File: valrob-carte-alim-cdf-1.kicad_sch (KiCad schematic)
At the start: 35 parts, among them J1 USB_C_Receptacle_USB2.0_14P, J26 Conn_01x02, J6 Conn_01x04_Pin, SW1 SW_Push, SW2 SW_Push, SW3 SW_Push, U3 SN65HVD230, U4 ESP32-S3-WROOM-1

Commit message: schem: complete BOM
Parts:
- C4: JLCPCB Part # C1525 -> C307331; Manufacturer Part Number CL05B104KO5NNNC -> CL05B104KB54PNC
- U4: Basic (none) -> Z; JLCPCB Part # (none) -> C2913204; Manufacturer (none) -> Espressif; Manufacturer Part Number (none) -> ESP32-S3-WROOM-1-N8R2
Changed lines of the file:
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@@
+			)
+		)
+		(property "Basic" "Z"
+			(at 137.16 104.14 0)
+			(effects
+				(font
+					(size 1.27 1.27)
+				)
+				(hide yes)
+			)
+		)
+		(property "JLCPCB Part #" "C2913204"
+			(at 137.16 104.14 0)
+			(effects
+				(font
+					(size 1.27 1.27)
+				)
+				(hide yes)
+			)
+		)
+		(property "Manufacturer" "Espressif"
+			(at 137.16 104.14 0)
+			(effects
+				(font
+					(size 1.27 1.27)
+				)
+				(hide yes)
+			)
+		)
+		(property "Manufacturer Part Number" "ESP32-S3-WROOM-1-N8R2"
+			(at 137.16 104.14 0)
+			(effects
+				(font
+					(size 1.27 1.27)
+				)
+				(hide yes)
 			)
 		)
@@
 			)
 		)
-		(property "JLCPCB Part #" "C1525"
+		(property "JLCPCB Part #" "C307331"
 			(at 127 181.61 0)
 			(effects
@@
 			)
 		)
-		(property "Manufacturer Part Number" "CL05B104KO5NNNC"
+		(property "Manufacturer Part Number" "CL05B104KB54PNC"
 			(at 127 181.61 0)
 			(effects

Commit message: schem: add sheet title
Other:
- company: (none) -> Valrobotik
- title: (none) -> Carte alim CDF 1
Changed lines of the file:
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@@
 	(generator_version "9.0")
 	(paper "A4")
+	(title_block
+		(title "Carte alim CDF 1")
+		(date "2026-01-15")
+		(rev "01")
+		(company "Valrobotik")
+	)
 	(rectangle
 		(start 15.24 119.38)

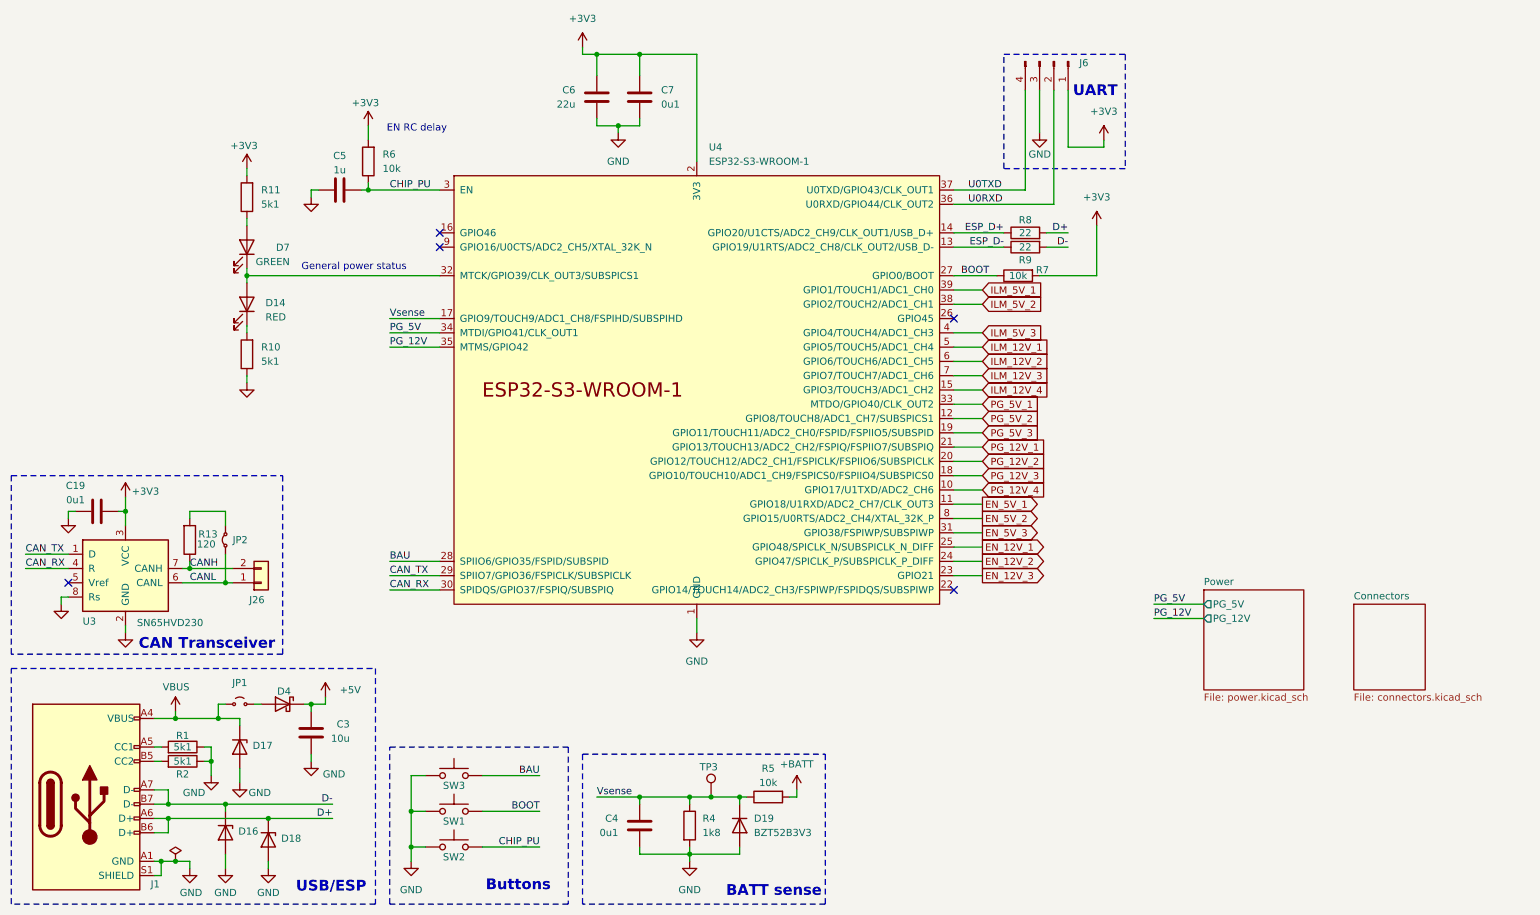
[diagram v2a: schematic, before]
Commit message: schem: renumber
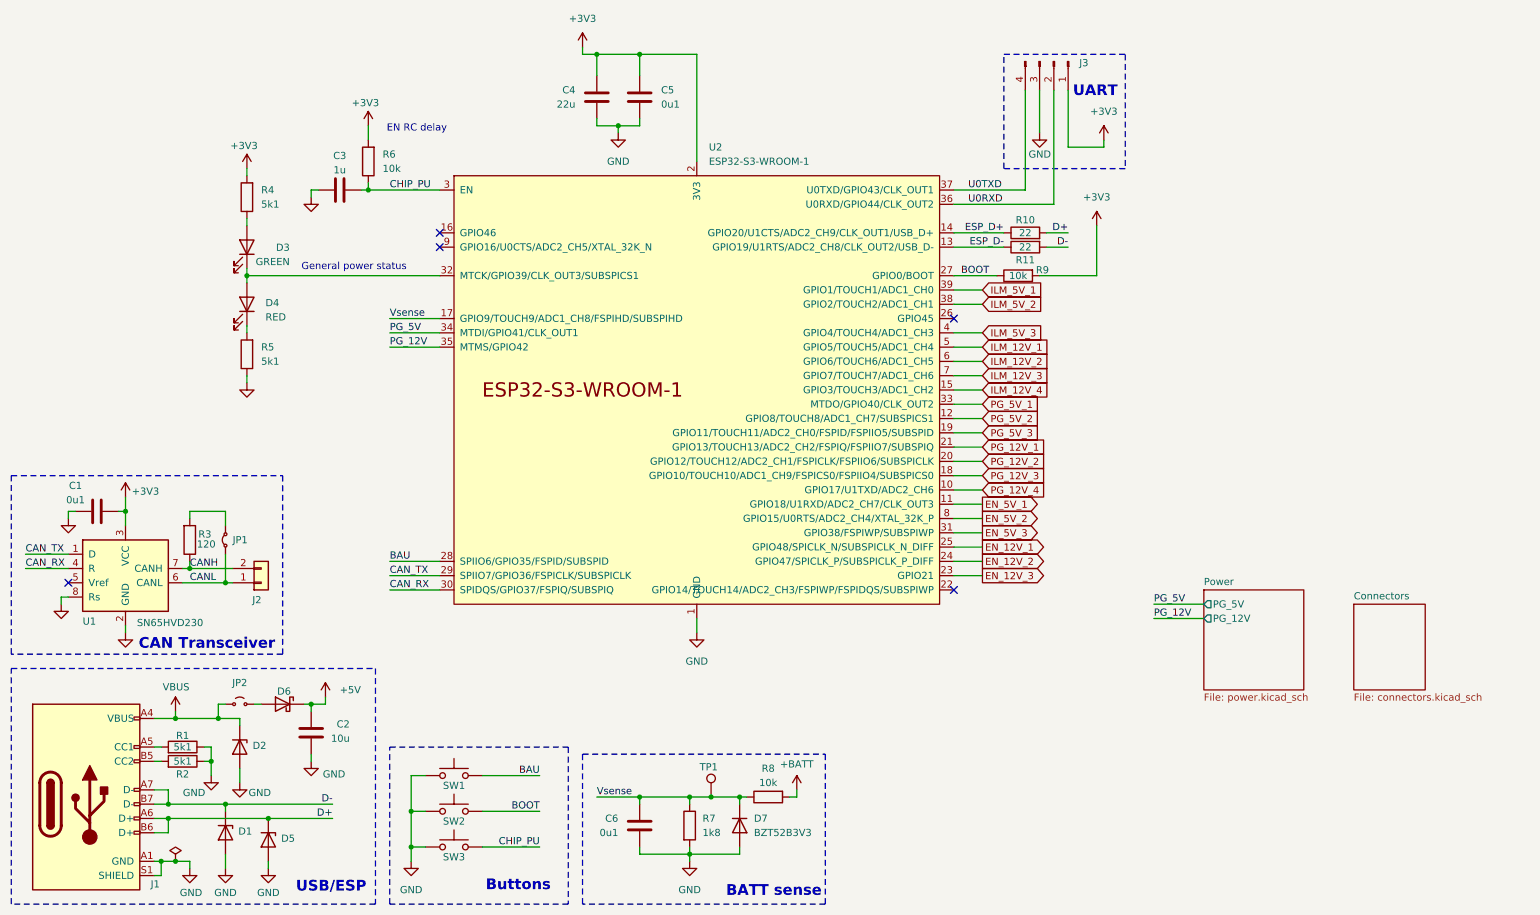
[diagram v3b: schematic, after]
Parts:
- renumbered C19 to C1, C3 to C2, C5 to C3, C6 to C4, C7 to C5, C4 to C6, D16 to D1, D17 to D2, D7 to D3, D14 to D4, D18 to D5, D4 to D6, D19 to D7, J26 to J2, J6 to J3, JP2 to JP1, JP1 to JP2, R8 to R10, R9 to R11, R13 to R3, R11 to R4, R10 to R5, R4 to R7, R5 to R8, R7 to R9, SW3 to SW1, SW1 to SW2, SW2 to SW3, TP3 to TP1, U3 to U1, U4 to U2

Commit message: pcb: add initial rough layout
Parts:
- SW2, SW3: footprint Connector_JST:JST_XH_B2B-XH-A_1x02_P2.50mm_Vertical -> Button_Switch_SMD:SW_SPST_TS-1088-xR020; Basic Z -> Y; JLCPCB Part # C158012 -> C720477; Manufacturer JST -> XUNPU; Manufacturer Part Number B2B-XH-A(LF)(SN) -> TS-1088-AR02016
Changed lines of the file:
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@@
-	)
-	(symbol
-		(lib_id "Switch:SW_Push")
-		(at 93.98 185.42 0)
-		(unit 1)
-		(exclude_from_sim no)
-		(in_bom yes)
-		(on_board yes)
-		(dnp no)
-		(property "Reference" "SW3"
-			(at 93.98 187.198 0)
-			(effects
-				(font
-					(size 1.27 1.27)
-				)
-			)
-		)
-		(property "Value" "SW_Push"
-			(at 93.98 180.34 0)
-			(effects
-				(font
-					(size 1.27 1.27)
-				)
-				(hide yes)
-			)
-		)
-		(property "Footprint" "Connector_JST:JST_XH_B2B-XH-A_1x02_P2.50mm_Vertical"
-			(at 93.98 180.34 0)
-			(effects
-				(font
-					(size 1.27 1.27)
-				)
-				(hide yes)
-			)
-		)
-		(property "Datasheet" "~"
-			(at 93.98 180.34 0)
-			(effects
-				(font
-					(size 1.27 1.27)
-				)
-				(hide yes)
-			)
-		)
-		(property "Description" "Push button switch, generic, two pins"
-			(at 93.98 185.42 0)
-			(effects
-				(font
-					(size 1.27 1.27)
-				)
-				(hide yes)
-			)
-		)
-		(property "Manufacturer" "JST"
-			(at 93.98 185.42 0)
-			(effects
-				(font
-					(size 1.27 1.27)
-				)
-				(hide yes)
-			)
-		)
-		(property "Manufacturer Part Number" "B2B-XH-A(LF)(SN)"
-			(at 93.98 185.42 0)
-			(effects
-				(font
-					(size 1.27 1.27)
-				)
-				(hide yes)
-			)
-		)
-		(property "Basic" "Z"
-			(at 93.98 185.42 0)
-			(effects
-				(font
-					(size 1.27 1.27)
-				)
-				(hide yes)
-			)
-		)
-		(property "JLCPCB Part #" "C158012"
-			(at 93.98 185.42 0)
-			(effects
-				(font
-					(size 1.27 1.27)
-				)
-				(hide yes)
-			)
-		)
-		(pin "2"
-		)
-		(pin "1"
-		)
-		(instances
-			(project "valrob-carte-alim-cdf-1"
-				(path "/8d7b287d-627f-46aa-8c27-0b5ed29ab4a2"
-					(reference "SW3")
-					(unit 1)
-				)
-			)
-		)
 	)
 	(symbol
@@
 	)
 	(symbol
+		(lib_id "Switch:SW_Push")
+		(at 93.98 179.07 0)
+		(unit 1)
+		(exclude_from_sim no)
+		(in_bom yes)
+		(on_board yes)
+		(dnp no)
+		(property "Reference" "SW2"
+			(at 93.98 180.848 0)
+			(effects
+				(font
+					(size 1.27 1.27)
+				)
+			)
+		)
+		(property "Value" "SW_Push"
+			(at 93.98 173.99 0)
+			(effects
+				(font
+					(size 1.27 1.27)
+				)
+				(hide yes)
+			)
+		)
+		(property "Footprint" "Button_Switch_SMD:SW_SPST_TS-1088-xR020"
+			(at 93.98 173.99 0)
+			(effects
+				(font
+					(size 1.27 1.27)
+				)
+				(hide yes)
+			)
+		)
+		(property "Datasheet" "~"
+			(at 93.98 173.99 0)
+			(effects
+				(font
+					(size 1.27 1.27)
+				)
+				(hide yes)
+			)
+		)
+		(property "Description" "Push button switch, generic, two pins"
+			(at 93.98 179.07 0)
+			(effects
+				(font
+					(size 1.27 1.27)
+				)
+				(hide yes)
+			)
+		)
+		(property "Manufacturer" "XUNPU"
+			(at 93.98 179.07 0)
+			(effects
+				(font
+					(size 1.27 1.27)
+				)
+				(hide yes)
+			)
+		)
+		(property "Manufacturer Part Number" "TS-1088-AR02016"
+			(at 93.98 179.07 0)
+			(effects
+				(font
+					(size 1.27 1.27)
+				)
+				(hide yes)
+			)
+		)
+		(property "Basic" "Y"
+			(at 93.98 179.07 0)
+			(effects
+				(font
+					(size 1.27 1.27)
+				)
+				(hide yes)
+			)
+		)
+		(property "JLCPCB Part #" "C720477"
+			(at 93.98 179.07 0)
+			(effects
+				(font
+					(size 1.27 1.27)
+				)
+				(hide yes)
+			)
+		)
+		(pin "2"
+		)
+		(pin "1"
+		)
+		(instances
+			(project "valrob-carte-alim-cdf-1"
+				(path "/8d7b287d-627f-46aa-8c27-0b5ed29ab4a2"
+					(reference "SW2")
+					(unit 1)
+				)
+			)
+		)
+	)
+	(symbol
 		(lib_id "Connector_Generic:Conn_01x02")
 		(at 59.69 138.43 0)
@@
 	)
 	(symbol
-		(lib_id "Switch:SW_Push")
-		(at 93.98 179.07 0)
-		(unit 1)
-		(exclude_from_sim no)
-		(in_bom yes)
-		(on_board yes)
-		(dnp no)
-		(property "Reference" "SW2"
-			(at 93.98 180.848 0)
-			(effects
-				(font
-					(size 1.27 1.27)
-				)
-			)
-		)
-		(property "Value" "SW_Push"
-			(at 93.98 173.99 0)
-			(effects
-				(font
-					(size 1.27 1.27)
-				)
-				(hide yes)
-			)
-		)
-		(property "Footprint" "Connector_JST:JST_XH_B2B-XH-A_1x02_P2.50mm_Vertical"
-			(at 93.98 173.99 0)
-			(effects
-				(font
-					(size 1.27 1.27)
-				)
-				(hide yes)
-			)
-		)
-		(property "Datasheet" "~"
-			(at 93.98 173.99 0)
-			(effects
-				(font
-					(size 1.27 1.27)
-				)
-				(hide yes)
-			)
-		)
-		(property "Description" "Push button switch, generic, two pins"
-			(at 93.98 179.07 0)
-			(effects
-				(font
-					(size 1.27 1.27)
-				)
-				(hide yes)
-			)
-		)
-		(property "Manufacturer" "JST"
-			(at 93.98 179.07 0)
-			(effects
-				(font
-					(size 1.27 1.27)
-				)
-				(hide yes)
-			)
-		)
-		(property "Manufacturer Part Number" "B2B-XH-A(LF)(SN)"
-			(at 93.98 179.07 0)
-			(effects
-				(font
-					(size 1.27 1.27)
-				)
-				(hide yes)
-			)
-		)
-		(property "Basic" "Z"
-			(at 93.98 179.07 0)
-			(effects
-				(font
-					(size 1.27 1.27)
-				)
-				(hide yes)
-			)
-		)
-		(property "JLCPCB Part #" "C158012"
-			(at 93.98 179.07 0)
-			(effects
-				(font
-					(size 1.27 1.27)
-				)
-				(hide yes)
-			)
-		)
-		(pin "2"
-		)
-		(pin "1"
-		)
-		(instances
-			(project "valrob-carte-alim-cdf-1"
-				(path "/8d7b287d-627f-46aa-8c27-0b5ed29ab4a2"
-					(reference "SW2")
-					(unit 1)
-				)
-			)
-		)
-	)
-	(symbol
 		(lib_id "power:GND")
 		(at 55.88 173.99 0)
@@
 					(unit 1)
 				)
+			)
+		)
+	)
+	(symbol
+		(lib_id "Switch:SW_Push")
+		(at 93.98 185.42 0)
+		(unit 1)
+		(exclude_from_sim no)
+		(in_bom yes)
+		(on_board yes)
+		(dnp no)
+		(property "Reference" "SW3"
+			(at 93.98 187.198 0)
+			(effects
+				(font
+					(size 1.27 1.27)
+				)
+			)
+		)
+		(property "Value" "SW_Push"
+			(at 93.98 180.34 0)
+			(effects
+				(font
+					(size 1.27 1.27)
+				)
+				(hide yes)
+			)
+		)
+		(property "Footprint" "Button_Switch_SMD:SW_SPST_TS-1088-xR020"
+			(at 93.98 180.34 0)
+			(effects
+				(font
+					(size 1.27 1.27)
+				)
+				(hide yes)
+			)
+		)
+		(property "Datasheet" "~"
+			(at 93.98 180.34 0)
+			(effects
+				(font
+					(size 1.27 1.27)
+				)
+				(hide yes)
+			)
+		)
+		(property "Description" "Push button switch, generic, two pins"
+			(at 93.98 185.42 0)
+			(effects
+				(font
+					(size 1.27 1.27)
+				)
+				(hide yes)
+			)
+		)
+		(property "Manufacturer" "XUNPU"
+			(at 93.98 185.42 0)
+			(effects
+				(font
+					(size 1.27 1.27)
+				)
+				(hide yes)
+			)
+		)
+		(property "Manufacturer Part Number" "TS-1088-AR02016"
+			(at 93.98 185.42 0)
+			(effects
+				(font
+					(size 1.27 1.27)
+				)
+				(hide yes)
+			)
+		)
+		(property "Basic" "Y"
+			(at 93.98 185.42 0)
+			(effects
+				(font
+					(size 1.27 1.27)
+				)
+				(hide yes)
+			)
+		)
+		(property "JLCPCB Part #" "C720477"
+			(at 93.98 185.42 0)
+			(effects
+				(font
+					(size 1.27 1.27)
+				)
+				(hide yes)
+			)
+		)
+		(pin "2"
+		)
+		(pin "1"
+		)
+		(instances
+			(project "valrob-carte-alim-cdf-1"
+				(path "/8d7b287d-627f-46aa-8c27-0b5ed29ab4a2"
+					(reference "SW3")
+					(unit 1)
+				)

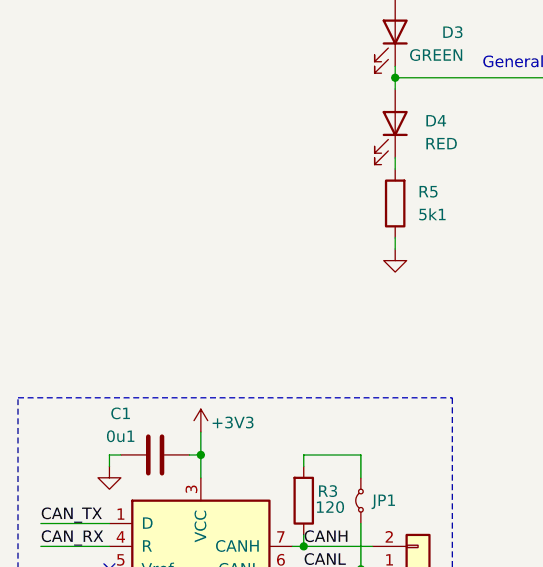
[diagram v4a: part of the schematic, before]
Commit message: schem: add mounting holes
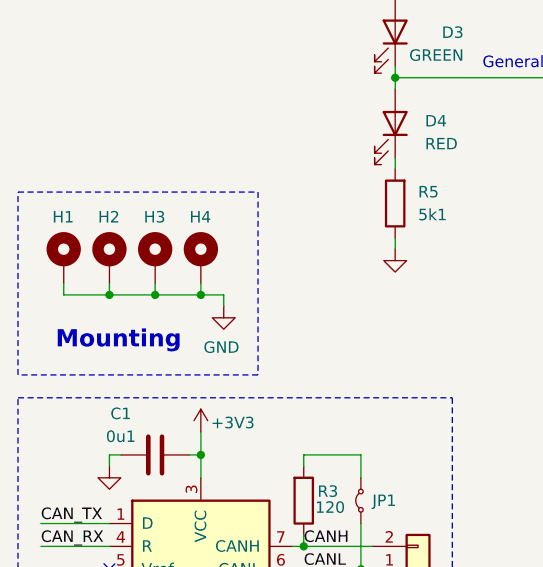
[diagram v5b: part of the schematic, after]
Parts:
- added H1, H2, H3, H4: MountingHole_Pad, MountingHole:MountingHole_2.2mm_M2_Pad_Via, symbol Mechanical:MountingHole_Pad
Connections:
- net GND: now also H1.1, H2.1, H3.1, H4.1
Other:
- note added: "Mounting"

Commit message: pcb: add can layout
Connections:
- net CAN_RX: now also U2.29 (SPIIO7/GPIO36/FSPICLK/SUBSPICLK); no longer U2.30 (SPIDQS/GPIO37/FSPIQ/SUBSPIQ)
- net CAN_TX: now also U2.30 (SPIDQS/GPIO37/FSPIQ/SUBSPIQ); no longer U2.29 (SPIIO7/GPIO36/FSPICLK/SUBSPICLK)
- net VBUS: no longer D2.1 (K)
- net at D6.2 (A), JP2.2 (B): now also D2.1 (K)
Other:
- moved on the sheet: JP2
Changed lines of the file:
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@@
 	)
 	(junction
-		(at 52.07 162.56)
-		(diameter 0)
-		(color 0 0 0 0)
-	)
-	(junction
 		(at 86.36 185.42)
 		(diameter 0)
@@
 	)
 	(junction
-		(at 44.45 162.56)
-		(diameter 0)
-		(color 0 0 0 0)
-	)
-	(junction
 		(at 46.99 135.89)
 		(diameter 0)
@@
 	)
 	(junction
+		(at 44.45 162.56)
+		(diameter 0)
+		(color 0 0 0 0)
+	)
+	(junction
 		(at 78.74 68.58)
 		(diameter 0)
@@
 		(color 0 0 0 0)
 	)
+	(junction
+		(at 55.88 162.56)
+		(diameter 0)
+		(color 0 0 0 0)
+	)
 	(no_connect
 		(at 91.44 76.2)
@@
 	(wire
 		(pts
-			(xy 52.07 160.02) (xy 53.34 160.02)
-		)
-		(stroke
-			(width 0)
-			(type default)
-		)
-	)
-	(wire
-		(pts
 			(xy 35.56 146.05) (xy 35.56 147.32)
 		)
@@
 	(wire
 		(pts
+			(xy 55.88 160.02) (xy 59.69 160.02)
+		)
+		(stroke
+			(width 0)
+			(type default)
+		)
+	)
+	(wire
+		(pts
 			(xy 182.88 114.3) (xy 187.96 114.3)
 		)
@@
 	(wire
 		(pts
+			(xy 82.55 137.16) (xy 91.44 137.16)
+		)
+		(stroke
+			(width 0)
+			(type default)
+		)
+	)
+	(wire
+		(pts
+			(xy 44.45 162.56) (xy 48.26 162.56)
+		)
+		(stroke
+			(width 0)
+			(type default)
+		)
+	)
+	(wire
+		(pts
 			(xy 154.94 175.26) (xy 154.94 176.53)
 		)
@@
 	(wire
 		(pts
+			(xy 82.55 139.7) (xy 91.44 139.7)
+		)
+		(stroke
+			(width 0)
+			(type default)
+		)
+	)
+	(wire
+		(pts
 			(xy 86.36 179.07) (xy 88.9 179.07)
 		)
@@
 	(wire
 		(pts
+			(xy 53.34 162.56) (xy 55.88 162.56)
+		)
+		(stroke
+			(width 0)
+			(type default)
+		)
+	)
+	(wire
+		(pts
 			(xy 127 44.45) (xy 127 48.26)
 		)
@@
 	(wire
 		(pts
-			(xy 20.32 107.95) (xy 20.32 106.68)
+			(xy 55.88 162.56) (xy 55.88 160.02)
 		)
 		(stroke
@@
 	(wire
 		(pts
-			(xy 35.56 125.73) (xy 35.56 128.27)
+			(xy 20.32 107.95) (xy 20.32 106.68)
 		)
 		(stroke
@@
 	(wire
 		(pts
-			(xy 43.18 182.88) (xy 43.18 180.34)
+			(xy 35.56 125.73) (xy 35.56 128.27)
 		)
 		(stroke
@@
 	(wire
 		(pts
-			(xy 119.38 55.88) (xy 119.38 57.15)
+			(xy 43.18 182.88) (xy 43.18 180.34)
 		)
 		(stroke
@@
 	(wire
 		(pts
-			(xy 135.89 186.69) (xy 144.78 186.69)
+			(xy 119.38 55.88) (xy 119.38 57.15)
 		)
 		(stroke
@@
 	(wire
 		(pts
-			(xy 78.74 68.58) (xy 91.44 68.58)
+			(xy 135.89 186.69) (xy 144.78 186.69)
 		)
 		(stroke
@@
 	(wire
 		(pts
-			(xy 127 176.53) (xy 135.89 176.53)
+			(xy 78.74 68.58) (xy 91.44 68.58)
 		)
 		(stroke
@@
 	(wire
 		(pts
-			(xy 52.07 160.02) (xy 52.07 162.56)
+			(xy 127 176.53) (xy 135.89 176.53)
 		)
 		(stroke
@@
 	(wire
 		(pts
-			(xy 58.42 160.02) (xy 59.69 160.02)
-		)
-		(stroke
-			(width 0)
-			(type default)
-		)
-	)
-	(wire
-		(pts
 			(xy 182.88 134.62) (xy 187.96 134.62)
 		)
@@
 	(wire
 		(pts
-			(xy 55.88 162.56) (xy 52.07 162.56)
-		)
-		(stroke
-			(width 0)
-			(type default)
-		)
-	)
-	(wire
-		(pts
 			(xy 127 44.45) (xy 137.16 44.45)
 		)
@@
 	(wire
 		(pts
-			(xy 82.55 139.7) (xy 91.44 139.7)
-		)
-		(stroke
-			(width 0)
-			(type default)
-		)
-	)
-	(wire
-		(pts
 			(xy 119.38 176.53) (xy 127 176.53)
 		)
@@
 	(wire
 		(pts
-			(xy 52.07 162.56) (xy 44.45 162.56)
-		)
-		(stroke
-			(width 0)
-			(type default)
-		)
-	)
-	(wire
-		(pts
 			(xy 53.34 128.27) (xy 53.34 125.73)
 		)
@@
 	(wire
 		(pts
-			(xy 82.55 137.16) (xy 91.44 137.16)
-		)
-		(stroke
-			(width 0)
-			(type default)
-		)
-	)
-	(wire
-		(pts
 			(xy 182.88 99.06) (xy 187.96 99.06)
 		)
@@
 		)
 	)
+	(label "CAN_RX"
+		(at 82.55 137.16 0)
+		(effects
+			(font
+				(size 1.27 1.27)
+			)
+			(justify left bottom)
+		)
+	)
 	(label "BAU"
 		(at 109.22 172.72 180)
@@
 		)
 	)
-	(label "CAN_TX"
-		(at 82.55 137.16 0)
-		(effects
-			(font
-				(size 1.27 1.27)
-			)
-			(justify left bottom)
-		)
-	)
 	(label "CAN_RX"
 		(at 17.78 135.89 0)
@@
 	)
 	(label "CAN_TX"
+		(at 82.55 139.7 0)
+		(effects
+			(font
+				(size 1.27 1.27)
+			)
+			(justify left bottom)
+		)
+	)
+	(label "CAN_TX"
 		(at 17.78 133.35 0)
 		(effects
@@
 		)
 	)
-	(label "CAN_RX"
-		(at 82.55 139.7 0)
-		(effects
-			(font
-				(size 1.27 1.27)
-			)
-			(justify left bottom)
-		)
-	)
 	(label "D-"
 		(at 203.2 78.74 180)
@@
 	(symbol
 		(lib_id "Jumper:Jumper_2_Small_Open")
-		(at 55.88 160.02 0)
+		(at 50.8 162.56 0)
 		(unit 1)
 		(exclude_from_sim no)
@@
 		(fields_autoplaced yes)
 		(property "Reference" "JP2"
-			(at 55.88 156.21 0)
+			(at 50.8 158.75 0)
 			(effects
 				(font
@@
 		)
 		(property "Value" "Jumper_2_Small_Open"
-			(at 55.88 156.21 0)
+			(at 50.8 158.75 0)
 			(effects
 				(font
@@
 		)
 		(property "Footprint" "Connector_PinHeader_2.54mm:PinHeader_2x01_P2.54mm_Vertical"
-			(at 55.88 160.02 0)
+			(at 50.8 162.56 0)
 			(effects
 				(font
@@
 		)
 		(property "Datasheet" "~"
-			(at 55.88 160.02 0)
+			(at 50.8 162.56 0)
 			(effects
 				(font
@@
 		)
 		(property "Description" "Jumper, 2-pole, small symbol, open"
-			(at 55.88 160.02 0)
+			(at 50.8 162.56 0)
 			(effects
 				(font

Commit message: pcb: add can routing
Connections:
- net BAU: now also U2.30 (SPIDQS/GPIO37/FSPIQ/SUBSPIQ); no longer U2.28 (SPIIO6/GPIO35/FSPID/SUBSPID)
- net CAN_RX: now also U2.28 (SPIIO6/GPIO35/FSPID/SUBSPID); no longer U2.29 (SPIIO7/GPIO36/FSPICLK/SUBSPICLK)
- net CAN_TX: now also U2.29 (SPIIO7/GPIO36/FSPICLK/SUBSPICLK); no longer U2.30 (SPIDQS/GPIO37/FSPIQ/SUBSPIQ)
